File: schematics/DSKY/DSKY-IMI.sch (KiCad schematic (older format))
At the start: 7 parts, among them J103 Conn_02x08, J104 Conn_02x10, U19 74LS04, U42 74LS04, U46 74LS04, U5 74LS04, U6 74LS00

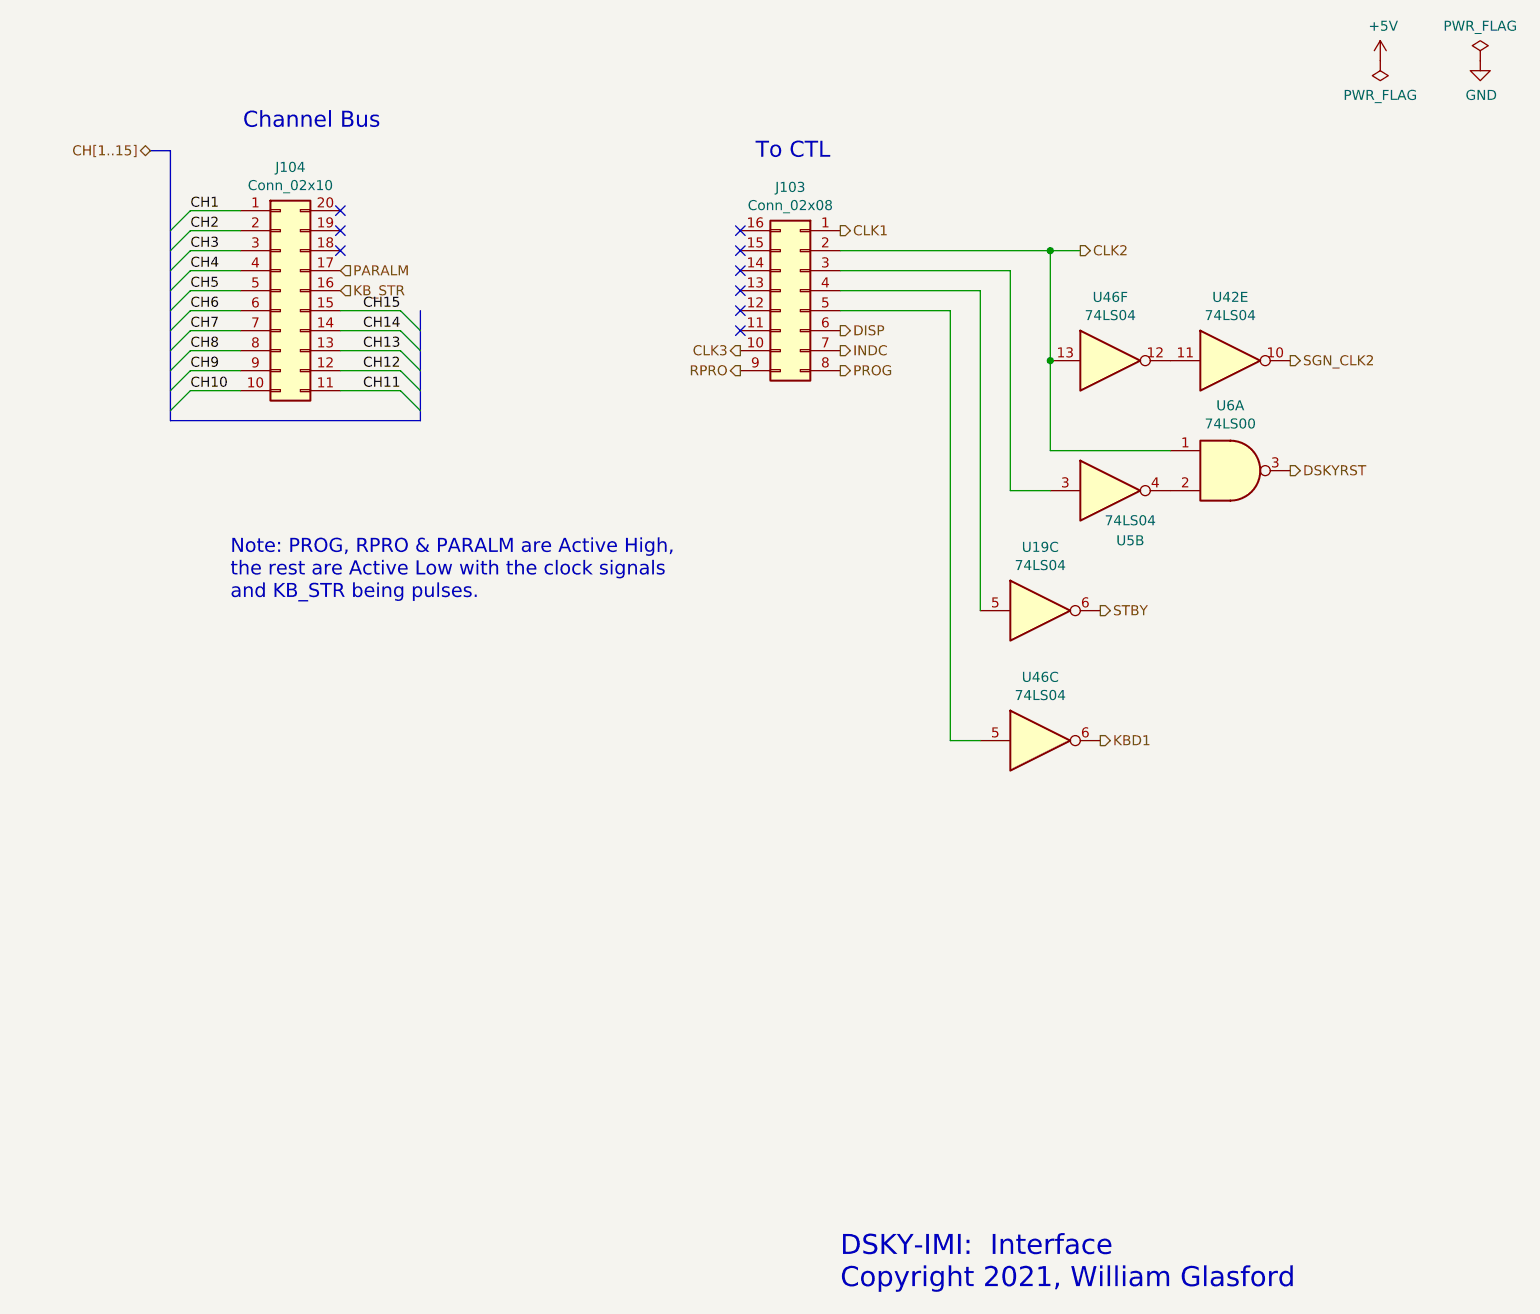
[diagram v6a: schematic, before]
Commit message: Added DSKY test schematic
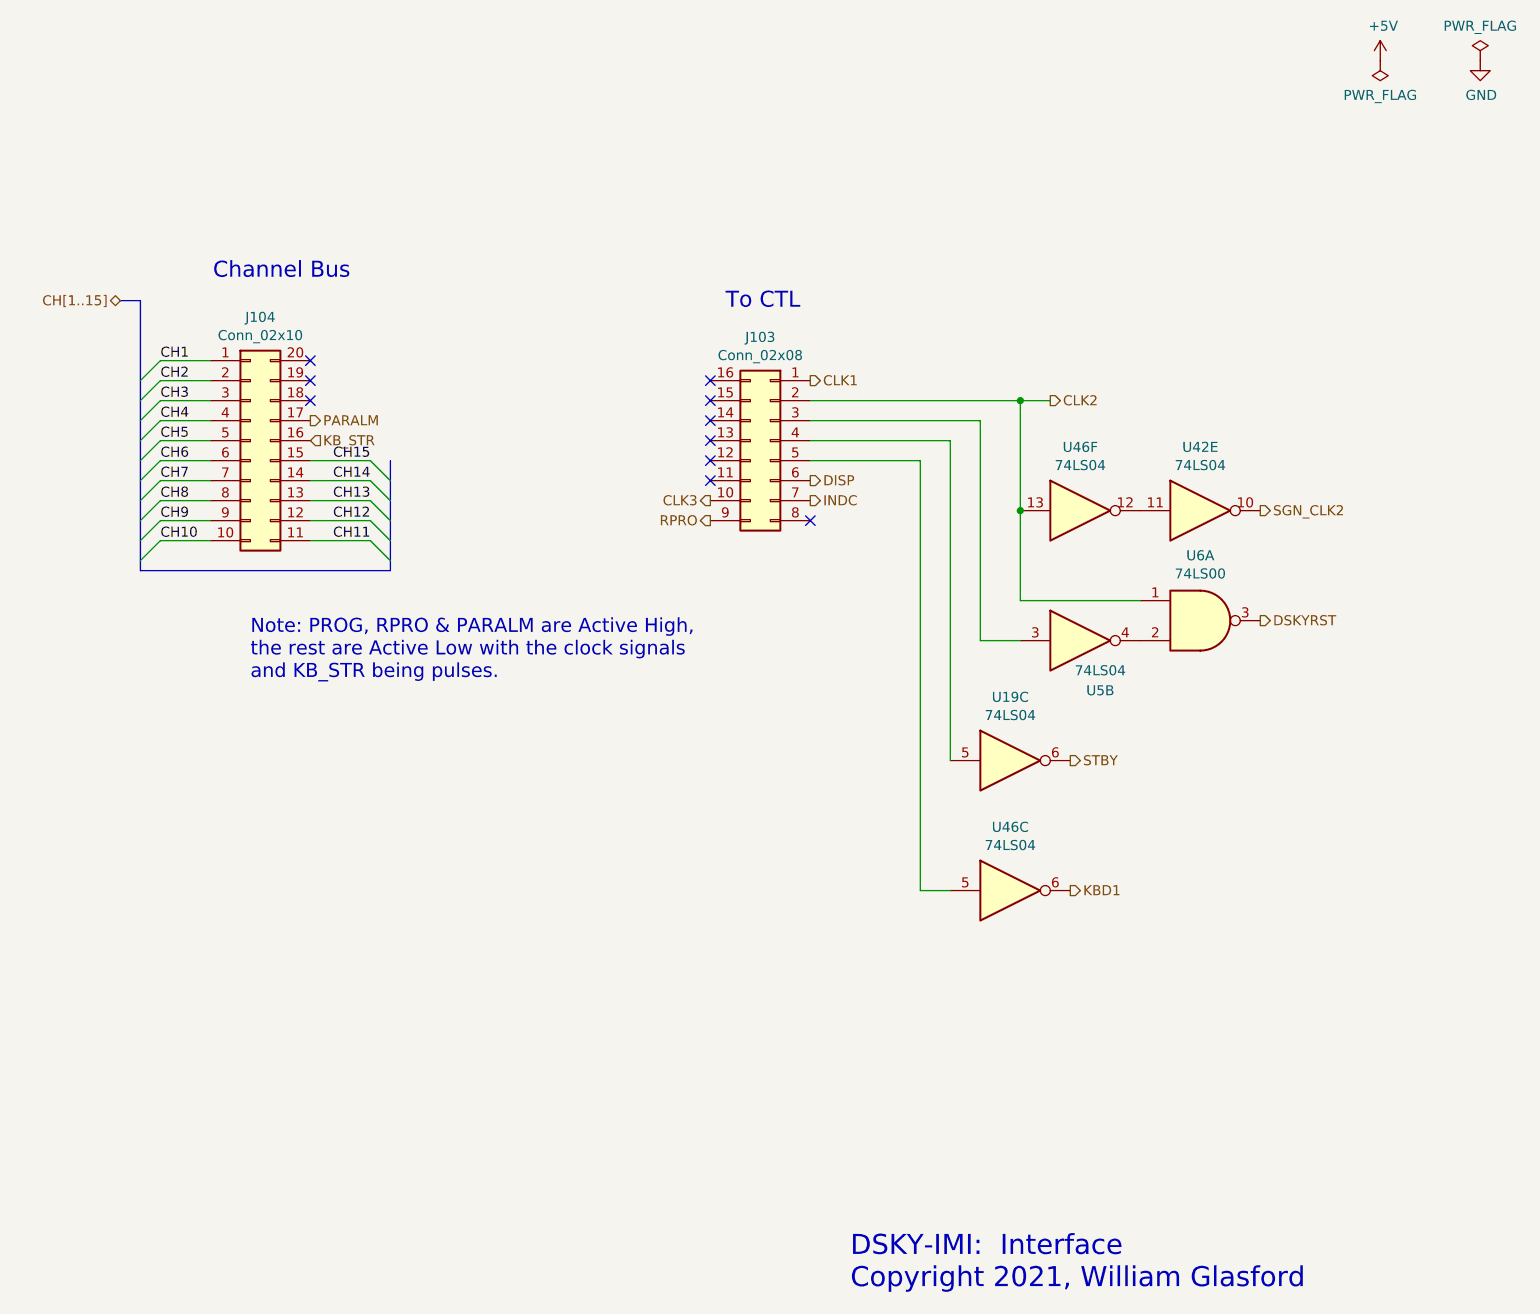
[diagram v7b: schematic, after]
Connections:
- net PROG: no longer names the net of J103.8 (Pin_8)
- no-connect marks 9 -> 10
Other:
- moved on the sheet: J103, J104, U19C, U42E, U46C, U46F, U5B, U6A

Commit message: DSKY Redesign
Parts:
- removed U19, U42, U46: 74LS04, symbol 74xx:74LS04
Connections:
- net KBD1: now also J103.5 (Pin_5)
- net STBY: now also J103.4 (Pin_4)
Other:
- moved on the sheet: U5B, U6A
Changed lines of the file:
@@
 $Descr A 11000 8500
 encoding utf-8
-Sheet 10 12
+Sheet 2 15
 Title ""
 Date ""
@@
 Wire Wire Line
 	3750 3000 4050 3000
-Text HLabel 7550 4500 2    50   Output ~ 0
+Text HLabel 6250 2900 2    50   Output ~ 0
 STBY
 Text HLabel 3750 2900 2    50   Input ~ 0
@@
 Text Notes 6200 2250 2    80   ~ 0
 To CTL
-Text HLabel 7550 5150 2    50   Output ~ 0
+Text HLabel 6250 3000 2    50   Output ~ 0
 KBD1
 Text HLabel 6250 3100 2    50   Output ~ 0
@@
 Text HLabel 6250 3200 2    50   Output ~ 0
 INDC
-NoConn ~ 5750 3100
 Text Notes 6450 7150 0    100  ~ 0
 DSKY-IMI:  Interface\nCopyright 2021, William Glasford
@@
 Text HLabel 5750 3300 0    50   Output ~ 0
 RPRO
-Text HLabel 8500 3800 2    50   Output ~ 0
+Text HLabel 8500 3050 2    50   Output ~ 0
 DSKYRST
 $Comp
 L 74xx:74LS00 U?
 U 1 1 6395652F
-P 8200 3800
+P 8200 3050
 AR Path="/5F5E4E3B/5F5F8347/6395652F" Ref="U?"  Part="1"
 AR Path="/60F98A72/6395652F" Ref="U?"  Part="1"
@@
 AR Path="/60F98A72/66CE2F9E/6395652F" Ref="U?"  Part="1"
 AR Path="/60F989FD/6395652F" Ref="U6"  Part="1"
-F 0 "U6" H 8200 4125 50  0000 C CNN
-F 1 "74LS00" H 8200 4034 50  0000 C CNN
-F 2 "" H 8200 3800 50  0001 C CNN
-F 3 "http://www.ti.com/lit/gpn/sn74ls00" H 8200 3800 50  0001 C CNN
-	1    8200 3800
+F 0 "U6" H 8200 3375 50  0000 C CNN
+F 1 "74LS00" H 8200 3284 50  0000 C CNN
+F 2 "" H 8200 3050 50  0001 C CNN
+F 3 "http://www.ti.com/lit/gpn/sn74ls00" H 8200 3050 50  0001 C CNN
+	1    8200 3050
 	1    0    0    -1
 $EndComp
@@
 L 74xx:74LS04 U?
 U 2 1 63956535
-P 7600 3900
+P 7600 3150
 AR Path="/5F5E4E3B/5F5F8347/63956535" Ref="U?"  Part="6"
 AR Path="/60F98A72/63956535" Ref="U?"  Part="2"
@@
 AR Path="/60F98A72/66CE2F9E/63956535" Ref="U?"  Part="6"
 AR Path="/60F989FD/63956535" Ref="U5"  Part="2"
-F 0 "U5" H 7700 3650 50  0000 C CNN
-F 1 "74LS04" H 7700 3750 50  0000 C CNN
-F 2 "" H 7600 3900 50  0001 C CNN
-F 3 "http://www.ti.com/lit/gpn/sn74LS04" H 7600 3900 50  0001 C CNN
-	2    7600 3900
+F 0 "U5" H 7700 2900 50  0000 C CNN
+F 1 "74LS04" H 7700 3000 50  0000 C CNN
+F 2 "" H 7600 3150 50  0001 C CNN
+F 3 "http://www.ti.com/lit/gpn/sn74LS04" H 7600 3150 50  0001 C CNN
+	2    7600 3150
 	1    0    0    -1
 $EndComp
@@
 	6250 2800 7100 2800
 Wire Wire Line
-	7100 2800 7100 3900
-Wire Wire Line
-	7100 3900 7300 3900
-$Comp
-L 74xx:74LS04 U42
-U 5 1 6247150B
-P 8200 3250
-F 0 "U42" H 8200 3567 50  0000 C CNN
-F 1 "74LS04" H 8200 3476 50  0000 C CNN
-F 2 "" H 8200 3250 50  0001 C CNN
-F 3 "http://www.ti.com/lit/gpn/sn74LS04" H 8200 3250 50  0001 C CNN
-	5    8200 3250
-	1    0    0    -1
-$EndComp
-$Comp
-L 74xx:74LS04 U46
-U 6 1 62471E0E
-P 7600 3250
-F 0 "U46" H 7600 3567 50  0000 C CNN
-F 1 "74LS04" H 7600 3476 50  0000 C CNN
-F 2 "" H 7600 3250 50  0001 C CNN
-F 3 "http://www.ti.com/lit/gpn/sn74LS04" H 7600 3250 50  0001 C CNN
-	6    7600 3250
-	1    0    0    -1
-$EndComp
+	7100 2800 7100 3150
+Wire Wire Line
+	7100 3150 7300 3150
 Wire Wire Line
 	6250 2700 7300 2700
@@
 	7450 2700 7300 2700
 Wire Wire Line
-	7300 3700 7900 3700
-Text HLabel 8500 3250 2    50   Output ~ 0
-SGN_CLK2
-Wire Wire Line
-	7300 2700 7300 3250
-Connection ~ 7300 3250
-Wire Wire Line
-	7300 3250 7300 3700
-Text Notes 3450 4100 0    70   ~ 0
+	7300 2950 7900 2950
+Text Notes 3350 4900 0    70   ~ 0
 Note: PROG, RPRO & PARALM are Active High,\nthe rest are Active Low with the clock signals\nand KB_STR being pulses.
-$Comp
-L 74xx:74LS04 U19
-U 3 1 61EE72FE
-P 7250 4500
-F 0 "U19" H 7250 4817 50  0000 C CNN
-F 1 "74LS04" H 7250 4726 50  0000 C CNN
-F 2 "" H 7250 4500 50  0001 C CNN
-F 3 "http://www.ti.com/lit/gpn/sn74LS04" H 7250 4500 50  0001 C CNN
-	3    7250 4500
-	1    0    0    -1
-$EndComp
-Wire Wire Line
-	6250 2900 6950 2900
-Wire Wire Line
-	6950 2900 6950 4500
-$Comp
-L 74xx:74LS04 U46
-U 3 1 61F122AA
-P 7250 5150
-F 0 "U46" H 7250 5467 50  0000 C CNN
-F 1 "74LS04" H 7250 5376 50  0000 C CNN
-F 2 "" H 7250 5150 50  0001 C CNN
-F 3 "http://www.ti.com/lit/gpn/sn74LS04" H 7250 5150 50  0001 C CNN
-	3    7250 5150
-	1    0    0    -1
-$EndComp
-Wire Wire Line
-	6250 3000 6800 3000
-Wire Wire Line
-	6800 3000 6800 5150
-Wire Wire Line
-	6800 5150 6950 5150
-Text HLabel 5750 3200 0    50   Output ~ 0
-CLK3
 Wire Bus Line
 	2900 3550 4150 3550
 Connection ~ 7300 2700
 NoConn ~ 6250 3300
+Wire Wire Line
+	7300 2700 7300 2950
+NoConn ~ 5750 3100
 Wire Bus Line
 	4150 3000 4150 3550
 Wire Bus Line
 	2900 2200 2900 3550
+Text HLabel 5750 3200 0    50   Output ~ 0
+CLK3
 $EndSCHEMATC
